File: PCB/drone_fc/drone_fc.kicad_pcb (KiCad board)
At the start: 4 copper layers, 35.1 x 37.6 mm, 7 parts, among them J1 USB_C_Receptacle_USB2.0_16P, Q1 BSS138, Q2 BSS138, U1 nRF52840, U2 USBLC6-2SC6, U3 ICM-20948, U4 MCP1703AT-3302E/DB

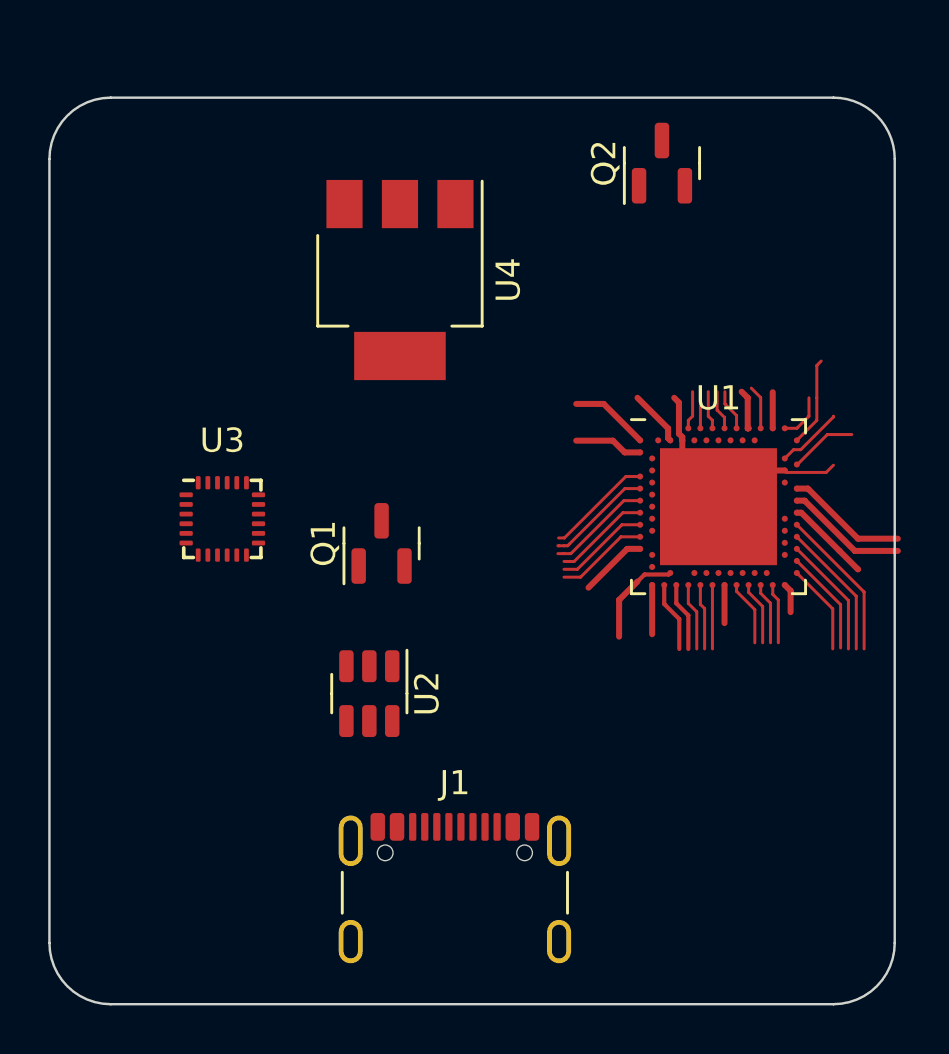
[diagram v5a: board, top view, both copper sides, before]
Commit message: Many new additions but importantly new MOSFETs for logic shifting (2 in 1 chip), some models to go with footprints on the JST connectors, and a footprint for battery power. Why did I choose such a small board size as my first real PCB
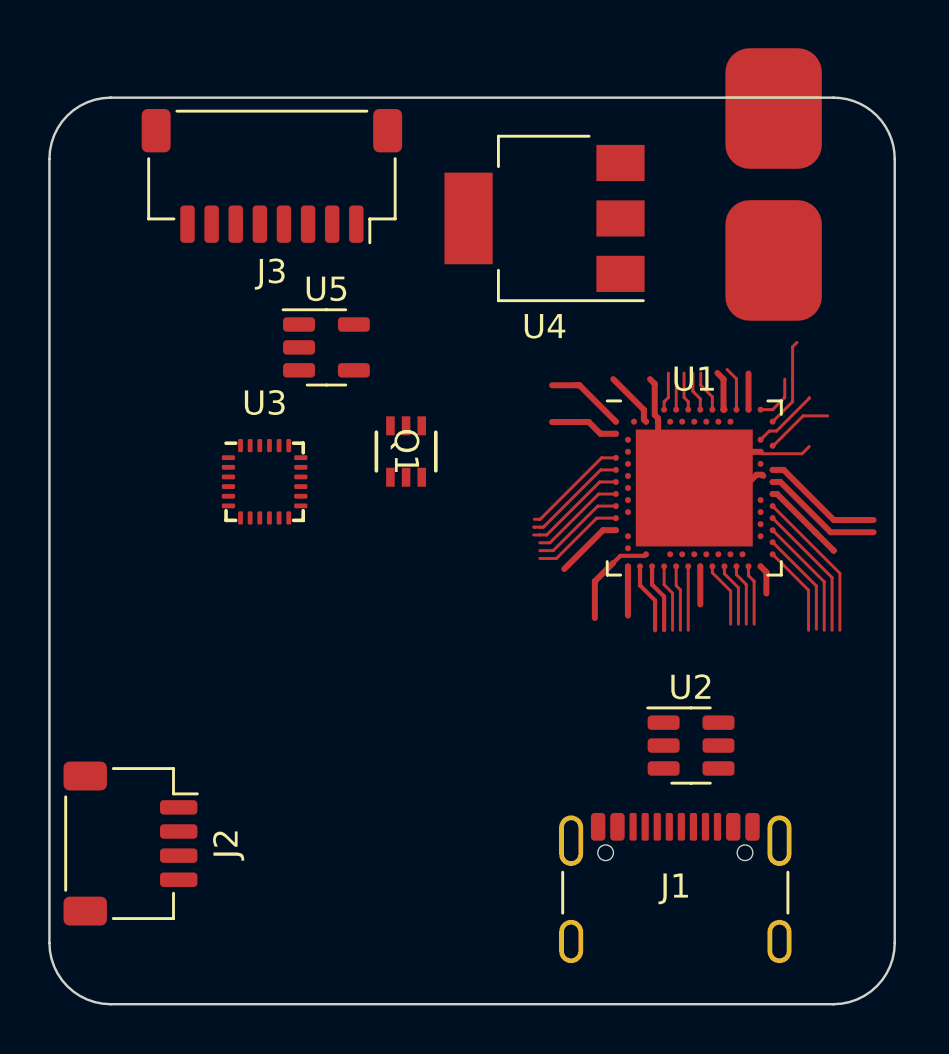
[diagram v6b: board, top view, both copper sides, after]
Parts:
- removed Q2: BSS138, Package_TO_SOT_SMD:SOT-23
- added BT1: Battery, MiscPads:Pad, F.Cu at (120.5, 52.7)
- added J2: Conn_01x04_Socket, Connector_JST:JST_SH_SM04B-SRSS-TB_1x04-1MP_P1.00mm_Horizontal, F.Cu at (97.0, 80.0)
- added J3: Conn_01x08_Socket, Connector_JST:JST_SH_SM08B-SRSS-TB_1x08-1MP_P1.00mm_Horizontal, F.Cu at (102.9, 52.3)
- added U5: LP5907MFX-1.8, Package_TO_SOT_SMD:SOT-23-5, F.Cu at (105.2, 59.4)
- Q1: value BSS138 -> BSD840N; footprint Package_TO_SOT_SMD:SOT-23 -> BSD840N:PG-SOT-363-DUAL-N_INF
- U1: footprint nRF52840:nRF52840 -> Package_DFN_QFN:Nordic_AQFN-73-1EP_7x7mm_P0.5mm
- moved U2 13.5 mm to (120.3, 75.9), turned to 0 degrees
- moved J1 9.14 mm to (119.6, 83.0)
- moved U4 6.52 mm to (114.2, 54.1), turned to 180 degrees
- moved Q1 3.94 mm to (108.5, 63.8), turned to -90 degrees
- moved U3 2.33 mm to (102.6, 65.0)
- moved U1 1.27 mm to (120.4, 65.3)
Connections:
- net /IMU_INT renamed /IMU_INT_1_8
- Q1 pad 1: Net-(Q1-G) -> /SDA
- Q1 pad 2: /SDA_1_8 -> +1V8
- Q1 pad 3: /SDA -> /SCL_1_8
- U1 pad G1: unconnected-(U1-P0.26-PadG1) -> /SDA
- U1 pad J1: unconnected-(U1-AIN2/P0.04-PadJ1) -> /SCL
- U3 pad 13: Net-(Q1-G) -> +1V8
- U3 pad 8: Net-(Q1-G) -> +1V8
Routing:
- net unconnected-(U1-P0.26-PadG1): track 4.44 -> 0.00 mm
- net /SDA: track 0.00 -> 4.44 mm
- net unconnected-(U1-AIN2/P0.04-PadJ1): track 4.39 -> 0.00 mm
- net /SCL: track 0.00 -> 4.39 mm
- net GND: track 10.8 -> 11.9 mm

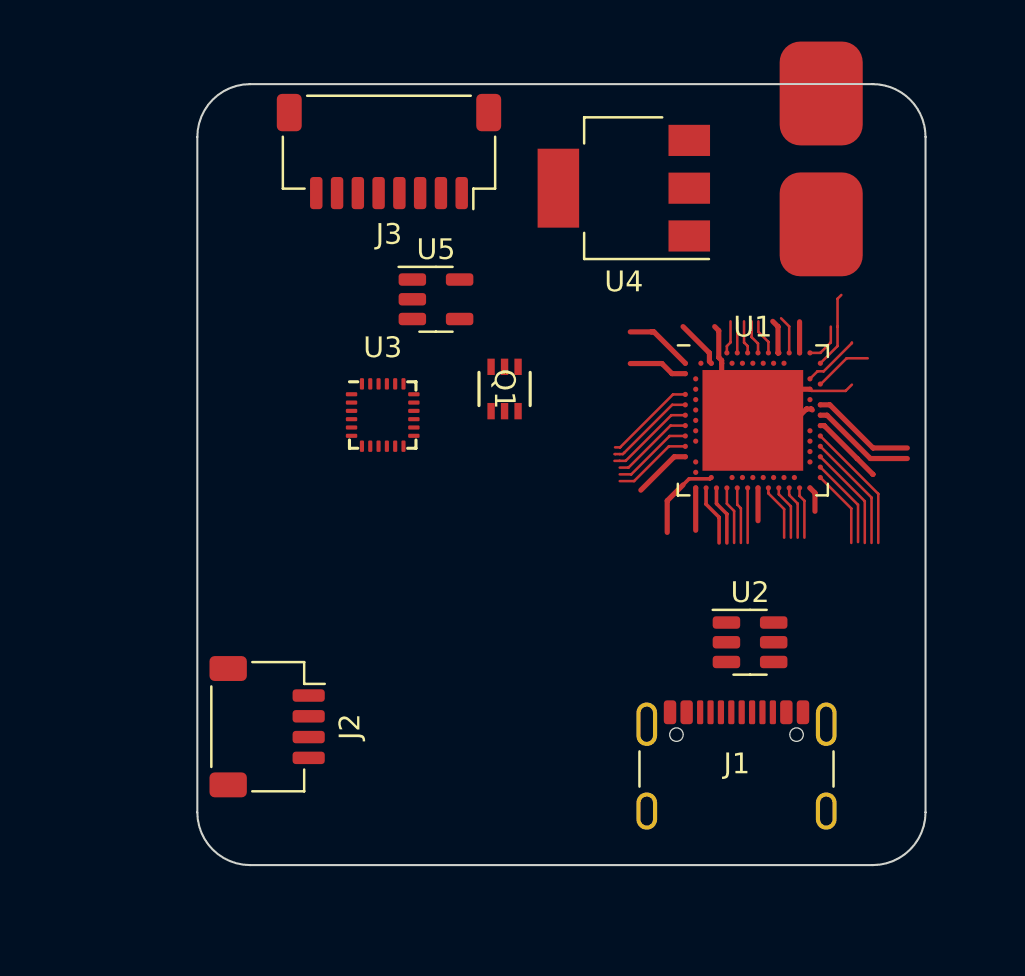
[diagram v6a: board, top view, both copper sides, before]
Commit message: New parts and footprints for existing resistors. Still some work to be done on checking battery voltage and PCB layout
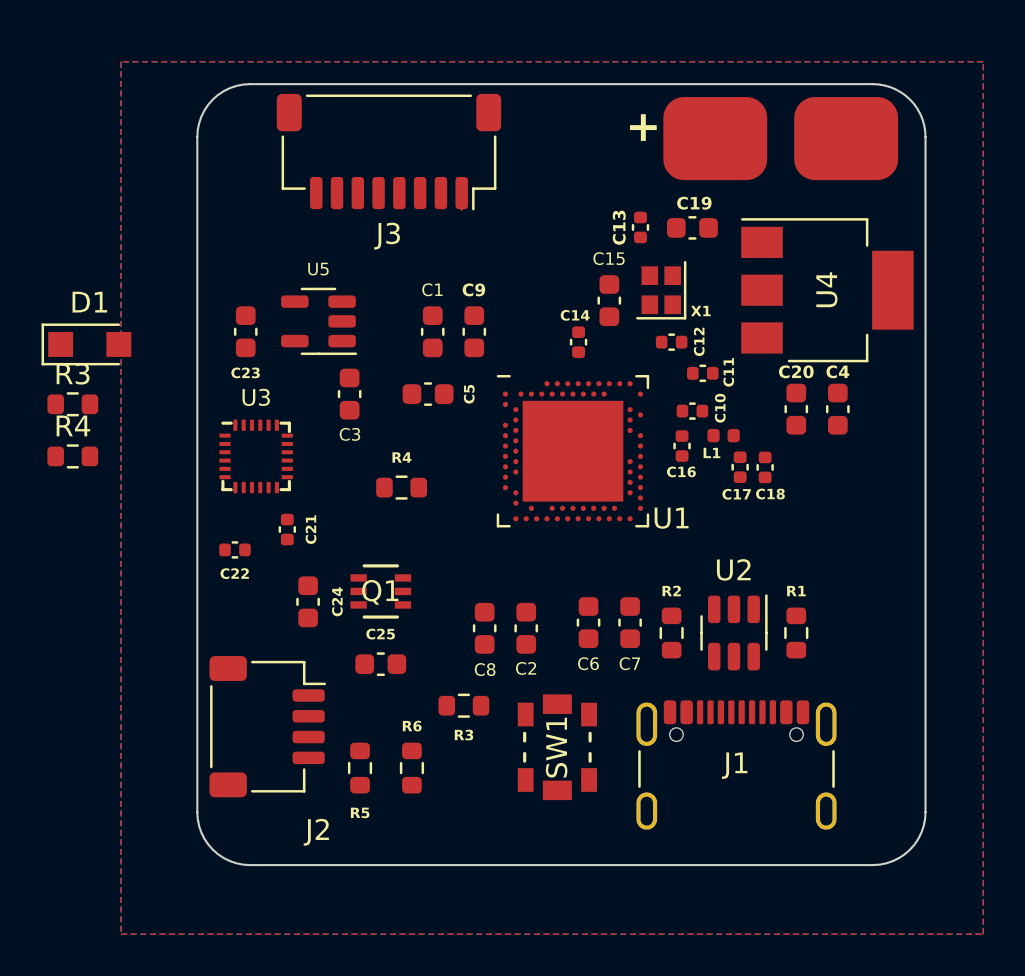
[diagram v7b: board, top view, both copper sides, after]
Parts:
- added C1: 1u, Capacitor_SMD:C_0603_1608Metric, F.Cu at (105.0, 61.0)
- added C10: NC, Capacitor_SMD:C_0402_1005Metric, F.Cu at (117.5, 64.8)
- added C11: 100p, Capacitor_SMD:C_0402_1005Metric, F.Cu at (118.0, 63.0)
- added C12: 12p, Capacitor_SMD:C_0402_1005Metric, F.Cu at (116.5, 61.5)
- added C13: 12p, Capacitor_SMD:C_0402_1005Metric, F.Cu at (115.0, 56.0)
- added C14: NC, Capacitor_SMD:C_0402_1005Metric, F.Cu at (112.0, 61.5)
- added C15: 1u, Capacitor_SMD:C_0603_1608Metric, F.Cu at (113.5, 59.5)
- added C16: 0p8, Capacitor_SMD:C_0402_1005Metric, F.Cu at (117.0, 66.5)
- added C17: 0p5, Capacitor_SMD:C_0402_1005Metric, F.Cu at (119.8, 67.5)
- added C18: NC, Capacitor_SMD:C_0402_1005Metric, F.Cu at (121.0, 67.5)
- added C19: 1u, Capacitor_SMD:C_0603_1608Metric, F.Cu at (117.5, 56.0)
- added C2: 4u7, Capacitor_SMD:C_0603_1608Metric, F.Cu at (109.5, 75.3)
- added C20: 1u, Capacitor_SMD:C_0603_1608Metric, F.Cu at (122.5, 64.7)
- added C21: 0u1, Capacitor_SMD:C_0402_1005Metric, F.Cu at (98.0, 70.5)
- added C22: 0u1, Capacitor_SMD:C_0402_1005Metric, F.Cu at (95.5, 71.5)
- added C23: 1u, Capacitor_SMD:C_0603_1608Metric, F.Cu at (96.0, 61.0)
- added C24: 1u, Capacitor_SMD:C_0603_1608Metric, F.Cu at (99.0, 74.0)
- added C25: 1u, Capacitor_SMD:C_0603_1608Metric, F.Cu at (102.5, 77.0)
- added C3: 1u, Capacitor_SMD:C_0603_1608Metric, F.Cu at (101.0, 64.0)
- added C4: 4u7, Capacitor_SMD:C_0603_1608Metric, F.Cu at (124.5, 64.7)
- added C5: 100n, Capacitor_SMD:C_0603_1608Metric, F.Cu at (104.8, 64.0)
- added C6: 100n, Capacitor_SMD:C_0603_1608Metric, F.Cu at (112.5, 75.0)
- added C7: 100n, Capacitor_SMD:C_0603_1608Metric, F.Cu at (114.5, 75.0)
- added C8: 4u7, Capacitor_SMD:C_0603_1608Metric, F.Cu at (107.5, 75.3)
- added C9: 1u, Capacitor_SMD:C_0603_1608Metric, F.Cu at (107.0, 61.0)
- added D1: D_Schottky, Diode_SMD:Nexperia_CFP3_SOD-123W, F.Cu at (88.5, 61.6)
- added L1: 4n7, Inductor_SMD:L_0402_1005Metric, F.Cu at (119.0, 66.0)
- added R1: 4k7, Resistor_SMD:R_0603_1608Metric, F.Cu at (122.5, 75.5)
- added R2: 4k7, Resistor_SMD:R_0603_1608Metric, F.Cu at (116.5, 75.5)
- added R3: 10k, Resistor_SMD:R_0603_1608Metric, F.Cu at (87.7, 64.5)
- added R3: 10k, Resistor_SMD:R_0603_1608Metric, F.Cu at (106.5, 79.0)
- added R4: 10k, Resistor_SMD:R_0603_1608Metric, F.Cu at (103.5, 68.5)
- added R4: 10k, Resistor_SMD:R_0603_1608Metric, F.Cu at (87.7, 67.0)
- added R5: 10k, Resistor_SMD:R_0603_1608Metric, F.Cu at (101.5, 82.0)
- added R6: 10k, Resistor_SMD:R_0603_1608Metric, F.Cu at (104.0, 82.0)
- added SW1: PTS820J25M, footprints:SW2_PTS820J25MSMTRLFS_CNK, F.Cu at (111.0, 81.0)
- added X1: 32MHz, Crystal:Crystal_SMD_2016-4Pin_2.0x1.6mm, F.Cu at (116.0, 59.0)
- moved Q1 11.4 mm to (102.5, 73.5), turned to 0 degrees
- moved U4 11.0 mm to (124.0, 59.0), turned to 0 degrees
- moved U1 8.78 mm to (111.8, 66.8)
- moved U3 6.41 mm to (96.5, 67.0)
- moved U5 5.76 mm to (99.5, 60.5), turned to 180 degrees
- moved BT1 2.53 mm to (121.8, 54.9), turned to 0 degrees
- moved U2 0.89 mm to (119.5, 75.5), turned to -90 degrees
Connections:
- U1 pad A10: unconnected-(U1-AIN5/P0.29-PadA10) -> /VBAT
- U1 pad A12: unconnected-(U1-AIN0/P0.02-PadA12) -> /M4
- U1 pad A14: unconnected-(U1-P1.15-PadA14) -> /M3
- U1 pad A16: unconnected-(U1-P1.13-PadA16) -> /M2
- U1 pad A20: unconnected-(U1-P1.10-PadA20) -> /M1
- U1 pad AA24: unconnected-(U1-SWDCLK-PadAA24) -> /SWDCLK
- U1 pad AC13: unconnected-(U1-P0.18/~{RESET}-PadAC13) -> Net-(U1-P0.18/~{RESET})
- U1 pad AC24: unconnected-(U1-SWDIO-PadAC24) -> /SWDIO
- U1 pad Y2: VBUS -> VDD
- U2 pad 1: /D+ -> /D-
- U2 pad 3: /D- -> /D+
- U2 pad 4: /DR- -> /DR+
- U2 pad 6: /DR+ -> /DR-
- U3 pad 23: /SCL_1_8 -> Net-(U3-SCL/SCLK)
- U3 pad 24: /SDA_1_8 -> Net-(U3-SDA/SDI)
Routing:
- net GND: track 11.9 -> 0.00 mm
- net VDD: track 10.4 -> 0.00 mm
- net unconnected-(U1-P1.06-PadR24): track 6.30 -> 0.00 mm
- net unconnected-(U1-P1.04-PadU24): track 5.67 -> 0.00 mm
- net /DEC4_6: track 5.12 -> 0.00 mm
- net unconnected-(U1-NFC1/P0.09-PadL24): track 5.05 -> 0.00 mm
- net unconnected-(U1-NFC2/P0.10-PadJ24): track 5.05 -> 0.00 mm
- net unconnected-(U1-P1.02-PadW24): track 5.04 -> 0.00 mm
- net /SDA: track 4.44 -> 0.00 mm
- net /SCL: track 4.39 -> 0.00 mm
- net unconnected-(U1-SWDCLK-PadAA24): track 4.36 -> 0.00 mm
- net unconnected-(U1-P0.06-PadL1): track 4.32 -> 0.00 mm
- net Net-(U1-DECUSB): track 4.11 -> 0.00 mm
- net unconnected-(U1-P0.08-PadN1): track 4.00 -> 0.00 mm
- net unconnected-(U1-TRACEDATA3/P1.09-PadR1): track 3.92 -> 0.00 mm
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- added copper zone on B.Cu, net GND
- added copper zone on F.Cu, net GND
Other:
- copper layers 4 -> 2
- board text added: "+"

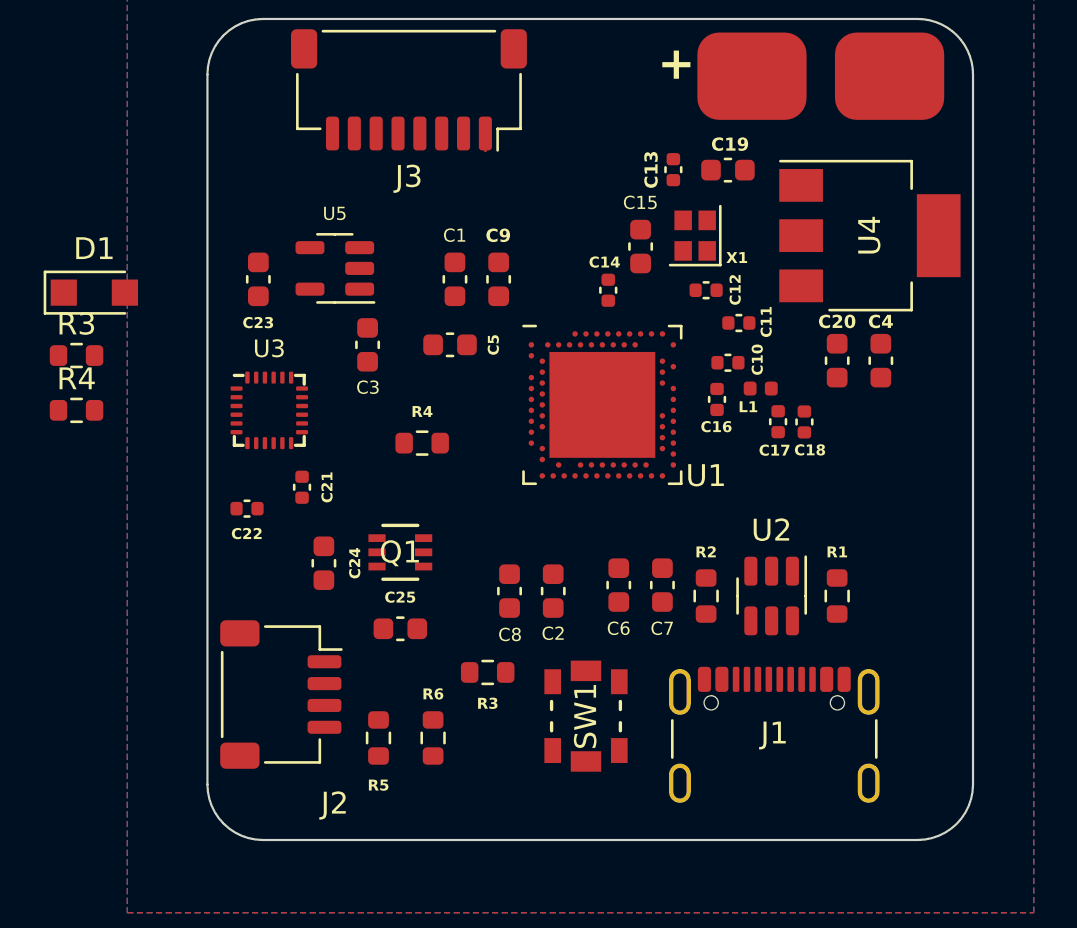
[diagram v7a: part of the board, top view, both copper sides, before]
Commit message: Back to the PCB now that I know the IMU works. I think most of the electrical connections are good (I'm still iffy on the nRF52840's VDD/VBUS stuff for hooking up a battery or USB), so I need to find components and run traces.
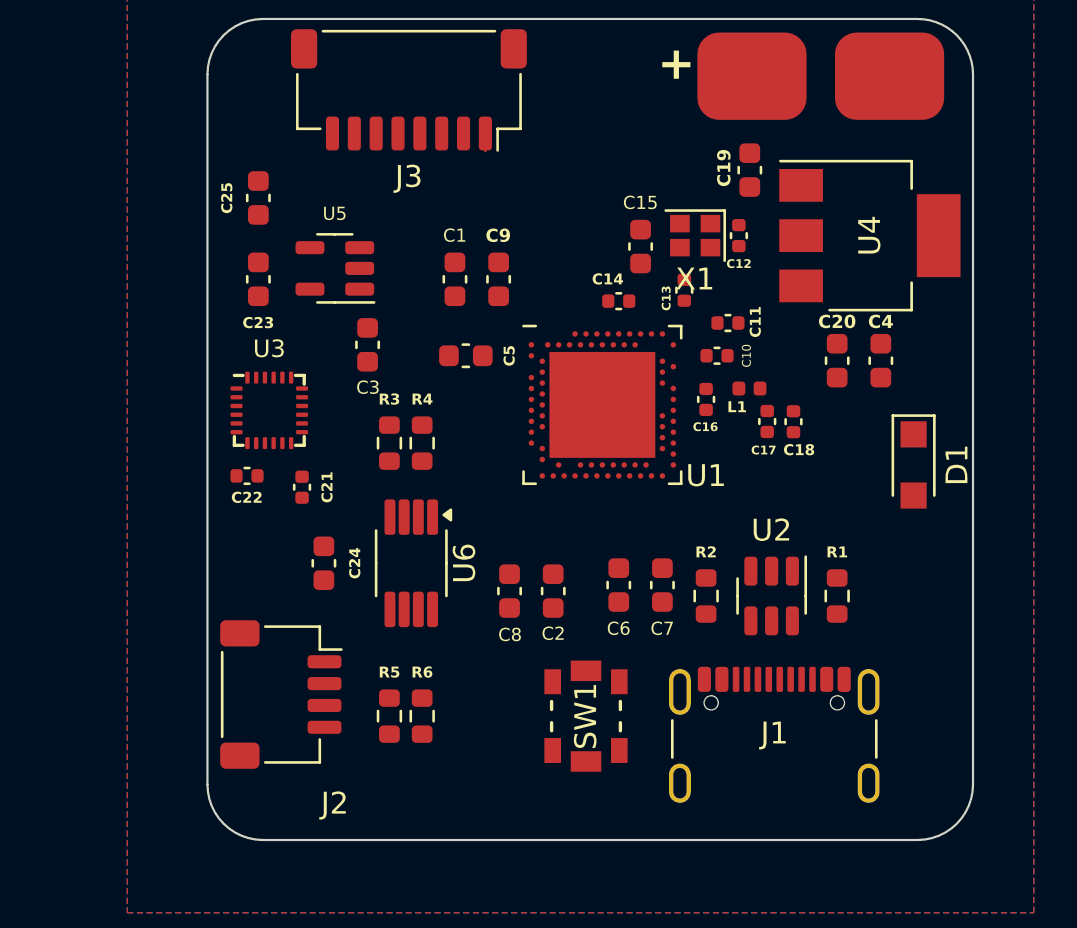
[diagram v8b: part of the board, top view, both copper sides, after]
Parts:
- removed Q1: BSD840N, BSD840N:PG-SOT-363-DUAL-N_INF
- removed the R3 at (106.5, 79.0)
- removed the R4 at (103.5, 68.5)
- added U6: TCA9517A, Package_SO:VSSOP-8_3x3mm_P0.65mm, F.Cu at (103.0, 74.0)
- moved D1 38.3 mm to (126.0, 69.5), turned to -90 degrees
- moved C25 20.8 mm to (96.0, 57.3), turned to 90 degrees
- moved R4 15.9 mm to (103.5, 68.5), turned to -90 degrees
- moved R3 14.9 mm to (102.0, 68.5), turned to 90 degrees
- moved C13 5.54 mm to (115.5, 61.5), turned to -90 degrees
- moved C12 2.92 mm to (118.0, 59.0), turned to 90 degrees
- moved C22 1.50 mm to (95.5, 70.0)
- moved R5 1.12 mm to (102.0, 81.0), turned to 90 degrees
- moved R6 1.12 mm to (103.5, 81.0)
- moved C19 1.00 mm to (118.5, 56.0), turned to -90 degrees
- moved C5 0.88 mm to (105.5, 64.5)
- moved C14 0.69 mm to (112.5, 62.0), turned to 180 degrees
- moved C10 0.59 mm to (117.0, 64.5)
- moved L1 0.52 mm to (118.5, 66.0)
- moved C17 0.50 mm to (119.3, 67.5)
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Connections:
- C1 pad 1: VDD -> 3V3
- C15 pad 1: VDD -> 3V3
- C20 pad 1: VDD -> 3V3
- C25 pad 1: VDD -> 3V3
- C3 pad 1: VDD -> 3V3
- C4 pad 1: VDD -> 3V3
- C6 pad 1: VDD -> 3V3
- C7 pad 1: VDD -> 3V3
- J2 pad 2: VDD -> 3V3
- J2 pad 3: /SCL -> /SDA
- J2 pad 4: /SDA -> /SCL
- U1 pad A22: VDD -> 3V3
- U1 pad AD14: VDD -> 3V3
- U1 pad AD23: VDD -> 3V3
- U1 pad B1: VDD -> 3V3
- U1 pad W1: VDD -> 3V3
- U1 pad Y2: VDD -> 3V3
- U2 pad 5: VDD -> 3V3
- U4 pad 3: VDD -> 3V3
- U5 pad 1: VDD -> 3V3
- U5 pad 3: VDD -> 3V3
- X1 pad 2: Net-(U1-XC2) -> (no net)
- X1 pad 3: (no net) -> Net-(U1-XC2)
